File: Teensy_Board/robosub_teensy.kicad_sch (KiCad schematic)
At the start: 51 parts, among them IC1 TEENSY_4.1, J1 Conn_01x03_Pin, J10 Conn_01x02_Pin, J11 Conn_01x02_Pin, J12 Conn_01x04_Pin, J13 Conn_01x04_Pin, J14 Conn_01x04_Pin, J15 Conn_01x04_Pin, J16 Conn_01x04_Pin, J17 Conn_01x04_Pin, J18 Conn_01x04_Pin, J19 Conn_01x04_Pin, J2 Conn_01x03_Pin, J20 Conn_01x04_Pin, J21 Conn_01x04_Pin, J22 Conn_01x06_Pin, J23 Conn_01x06_Pin, J24 Conn_01x06_Pin, J25 Conn_01x01_Pin, J26 Conn_01x01_Pin, J27 Conn_01x01_Pin, J28 Conn_01x01_Pin, J29 Conn_01x01_Pin, J3 Conn_01x03_Pin, J30 Conn_01x01_Pin, J31 Conn_01x01_Pin, J32 Conn_01x01_Pin, J33 Conn_01x01_Pin, J34 Conn_01x01_Pin, J35 Conn_01x01_Pin, J36 Conn_01x01_Pin, J37 Conn_01x01_Pin, J38 Conn_01x01_Pin, J39 Conn_01x01_Pin, J4 Conn_01x03_Pin, J40 Conn_01x01_Pin, J41 Conn_01x01_Pin, J42 Conn_01x01_Pin, J43 Conn_01x01_Pin, J44 Conn_01x01_Pin, J45 Conn_01x01_Pin, J46 Conn_01x01_Pin, J47 Conn_01x01_Pin, J48 Conn_01x10_Pin, J49 Conn_01x10_Pin, J5 Conn_01x03_Pin, J50 Conn_01x10_Pin, J6 Conn_01x03_Pin, J7 Conn_01x03_Pin, J8 Conn_01x03_Pin, J9 Conn_01x02_Pin

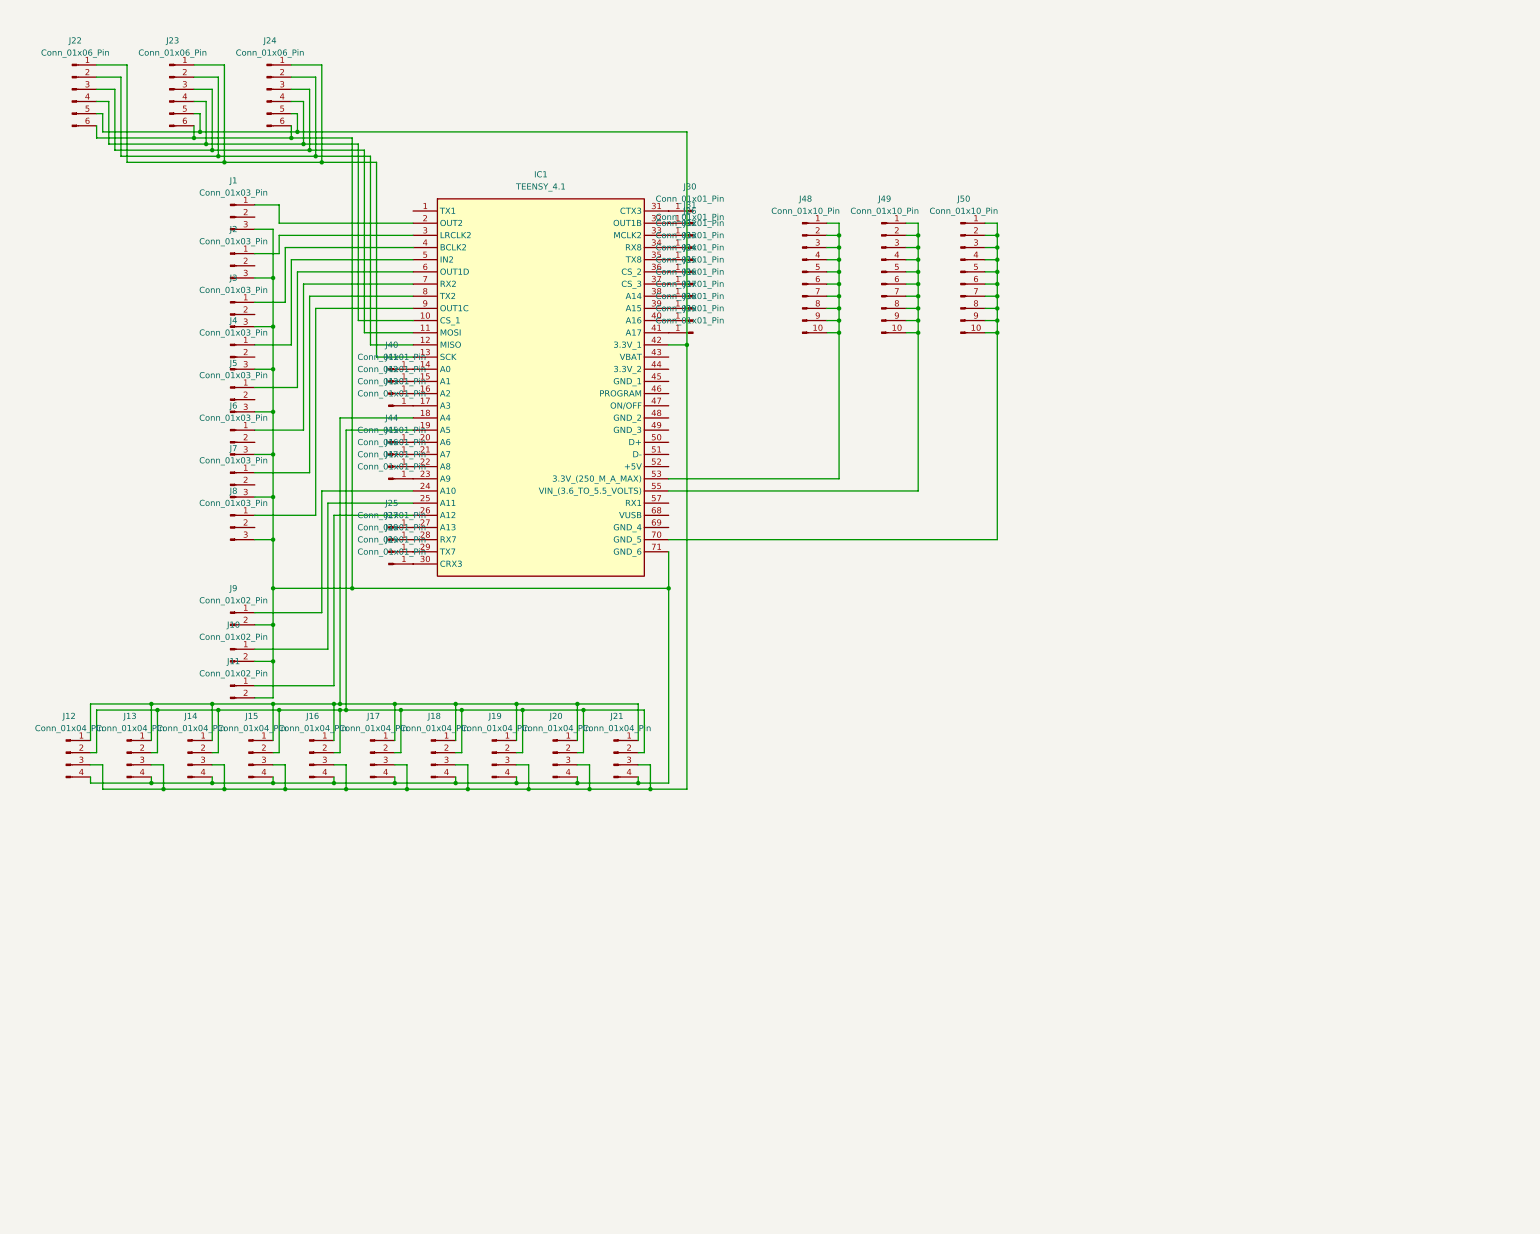
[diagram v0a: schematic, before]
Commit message: teensy board schematic
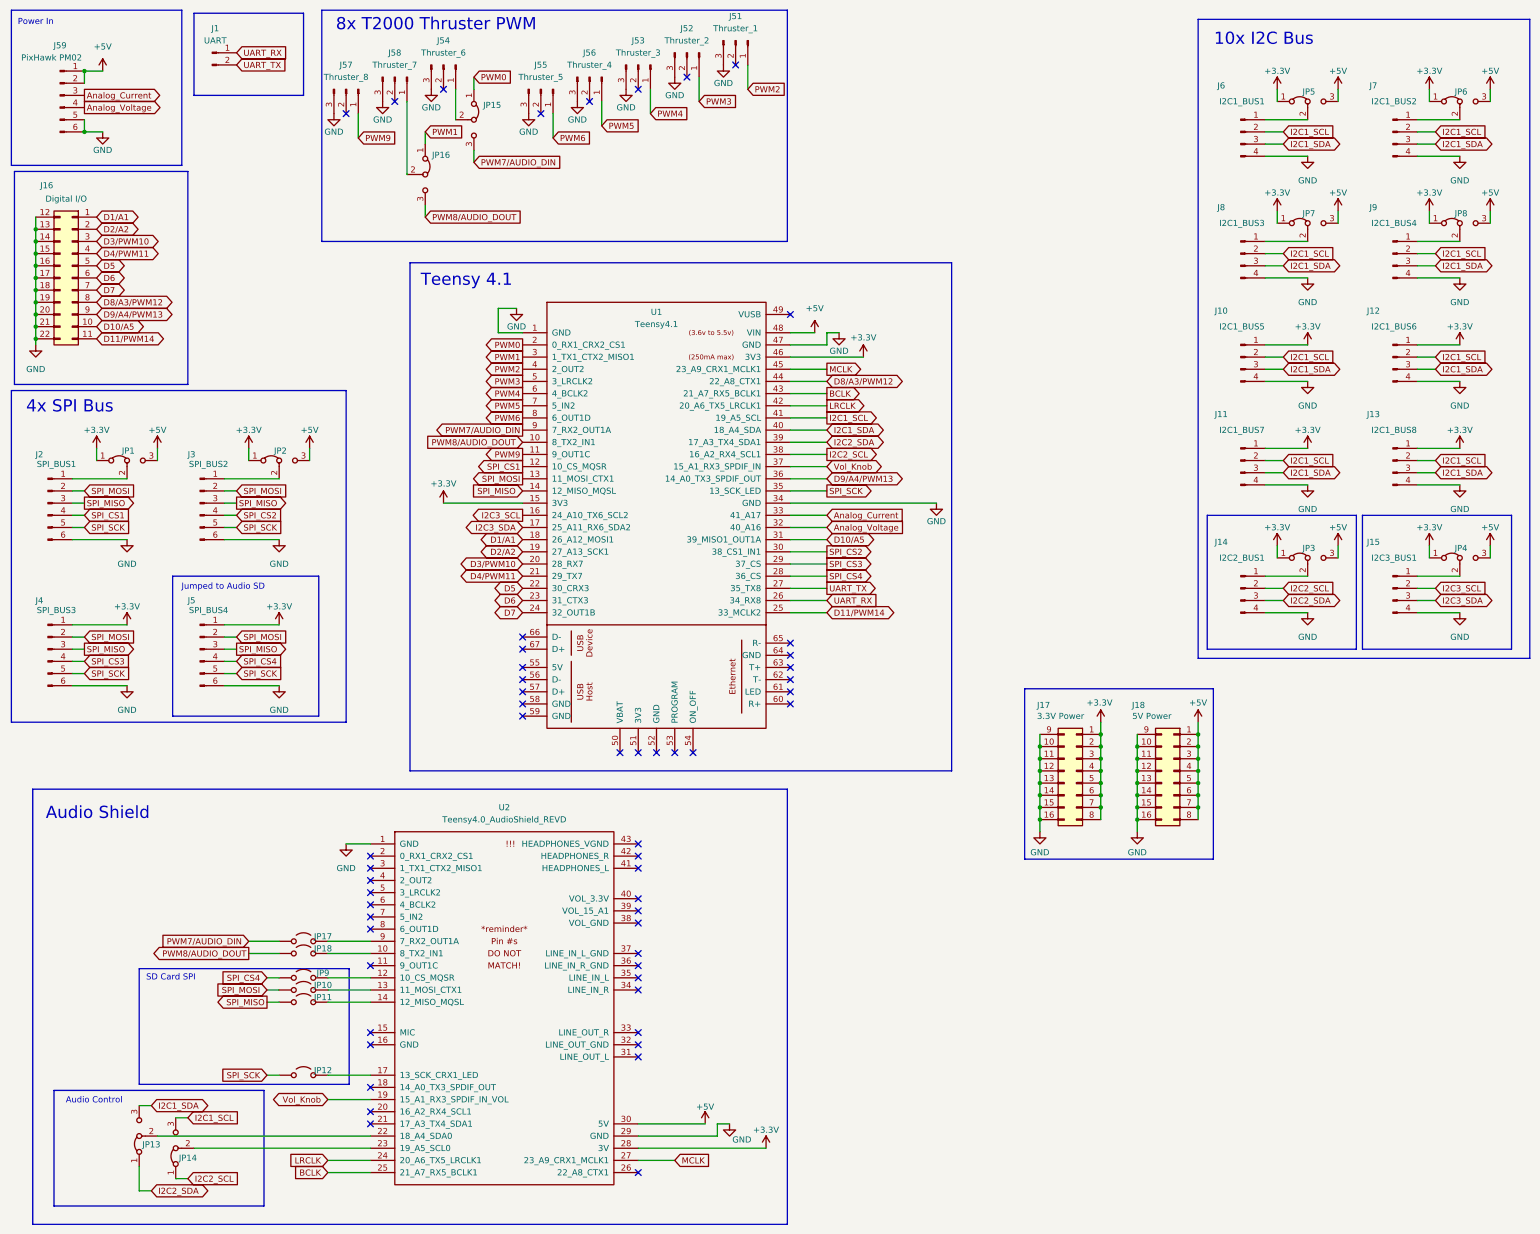
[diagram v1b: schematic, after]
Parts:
- removed IC1: TEENSY_4.1, KiCad:TEENSY41, symbol TEENSY_4_1:TEENSY_4.1
- removed J1, J2, J3, J4, J5, J6, J7, J8: Conn_01x03_Pin, Connector_PinSocket_2.54mm:PinSocket_1x03_P2.54mm_Vertical, symbol Connector:Conn_01x03_Pin
- removed J10, J11, J9: Conn_01x02_Pin, Connector_PinSocket_2.54mm:PinSocket_1x02_P2.54mm_Vertical, symbol Connector:Conn_01x02_Pin
- removed J16, J17, J18, J19, J20, J21: Conn_01x04_Pin, Connector_PinSocket_2.54mm:PinSocket_1x04_P2.54mm_Vertical, symbol Connector:Conn_01x04_Pin
- removed J22, J23, J24: Conn_01x06_Pin, Connector_PinSocket_2.54mm:PinSocket_1x06_P2.54mm_Vertical, symbol Connector:Conn_01x06_Pin
- removed J25, J26, J27, J28, J29, J30, J31, J32, J33, J34, J35, J36, J37, J38, J39, J40, J41, J42, J43, J44, J45, J46, J47: Conn_01x01_Pin, Connector_PinSocket_2.54mm:PinSocket_1x01_P2.54mm_Vertical, symbol Connector:Conn_01x01_Pin
- removed J48, J49, J50: Conn_01x10_Pin, Connector_PinSocket_2.54mm:PinSocket_1x10_P2.54mm_Vertical, symbol Connector:Conn_01x10_Pin
- added J1: UART, Connector_PinSocket_2.54mm:PinSocket_1x02_P2.54mm_Vertical, symbol Connector:Conn_01x02_Pin
- added J10: I2C1_BUS5, Connector_PinSocket_2.54mm:PinSocket_1x04_P2.54mm_Vertical, symbol Connector:Conn_01x04_Pin
- added J11: I2C1_BUS7, Connector_PinSocket_2.54mm:PinSocket_1x04_P2.54mm_Vertical, symbol Connector:Conn_01x04_Pin
- added J16: Digital I/O, symbol Connector_Generic:Conn_02x11_Top_Bottom
- added J17: 3.3V Power, Connector_PinSocket_2.54mm:PinSocket_2x08_P2.54mm_Vertical, symbol Connector_Generic:Conn_02x08_Top_Bottom
- added J18: 5V Power, Connector_PinSocket_2.54mm:PinSocket_2x08_P2.54mm_Vertical, symbol Connector_Generic:Conn_02x08_Top_Bottom
- added J2: SPI_BUS1, Connector_PinSocket_2.54mm:PinSocket_1x06_P2.54mm_Vertical, symbol Connector:Conn_01x06_Pin
- added J3: SPI_BUS2, Connector_PinSocket_2.54mm:PinSocket_1x06_P2.54mm_Vertical, symbol Connector:Conn_01x06_Pin
- added J4: SPI_BUS3, Connector_PinSocket_2.54mm:PinSocket_1x06_P2.54mm_Vertical, symbol Connector:Conn_01x06_Pin
- added J5: SPI_BUS4, Connector_PinSocket_2.54mm:PinSocket_1x06_P2.54mm_Vertical, symbol Connector:Conn_01x06_Pin
- added J51: Thruster_1, Connector_PinSocket_2.54mm:PinSocket_1x03_P2.54mm_Vertical, symbol Connector:Conn_01x03_Pin
- added J52: Thruster_2, Connector_PinSocket_2.54mm:PinSocket_1x03_P2.54mm_Vertical, symbol Connector:Conn_01x03_Pin
- added J53: Thruster_3, Connector_PinSocket_2.54mm:PinSocket_1x03_P2.54mm_Vertical, symbol Connector:Conn_01x03_Pin
- added J54: Thruster_6, Connector_PinSocket_2.54mm:PinSocket_1x03_P2.54mm_Vertical, symbol Connector:Conn_01x03_Pin
- added J55: Thruster_5, Connector_PinSocket_2.54mm:PinSocket_1x03_P2.54mm_Vertical, symbol Connector:Conn_01x03_Pin
- added J56: Thruster_4, Connector_PinSocket_2.54mm:PinSocket_1x03_P2.54mm_Vertical, symbol Connector:Conn_01x03_Pin
- added J57: Thruster_8, Connector_PinSocket_2.54mm:PinSocket_1x03_P2.54mm_Vertical, symbol Connector:Conn_01x03_Pin
- added J58: Thruster_7, Connector_PinSocket_2.54mm:PinSocket_1x03_P2.54mm_Vertical, symbol Connector:Conn_01x03_Pin
- added J59: PixHawk PM02, Connector_PinSocket_2.54mm:PinSocket_1x06_P2.54mm_Vertical, symbol Connector:Conn_01x06_Pin
- added J6: I2C1_BUS1, Connector_PinSocket_2.54mm:PinSocket_1x04_P2.54mm_Vertical, symbol Connector:Conn_01x04_Pin
- added J7: I2C1_BUS2, Connector_PinSocket_2.54mm:PinSocket_1x04_P2.54mm_Vertical, symbol Connector:Conn_01x04_Pin
- added J8: I2C1_BUS3, Connector_PinSocket_2.54mm:PinSocket_1x04_P2.54mm_Vertical, symbol Connector:Conn_01x04_Pin
- added J9: I2C1_BUS4, Connector_PinSocket_2.54mm:PinSocket_1x04_P2.54mm_Vertical, symbol Connector:Conn_01x04_Pin
- added JP1, JP13, JP14, JP15, JP16, JP2, JP3, JP4, JP5, JP6, JP7, JP8: Jumper_3_Bridged12, Connector_PinSocket_2.54mm:PinSocket_1x03_P2.54mm_Vertical, symbol Jumper:Jumper_3_Bridged12
- added JP10, JP11, JP12, JP17, JP18, JP9: Jumper_2_Open, Connector_PinSocket_2.54mm:PinSocket_1x02_P2.54mm_Vertical, symbol Jumper:Jumper_2_Open
- added U1: Teensy4.1, teensy:Teensy41, symbol teensy:Teensy4.1
- added U2: Teensy4.0_AudioShield_REVD, teensy_audio_shield:4.0audioshield, symbol teensy4.0_audioshield_revd:Teensy4.0_AudioShield_REVD
- J12: value Conn_01x04_Pin -> I2C1_BUS6
- J13: value Conn_01x04_Pin -> I2C1_BUS8
- J14: value Conn_01x04_Pin -> I2C2_BUS1
- J15: value Conn_01x04_Pin -> I2C3_BUS1
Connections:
- net +3.3V: now reaches J12.1 (Pin_1), J13.1 (Pin_1)
- net +3.3V: now also J10.1 (Pin_1), J11.1 (Pin_1), J17.1 (Pin_1), J17.2 (Pin_2), J17.3 (Pin_3), J17.4 (Pin_4), J17.5 (Pin_5), J17.6 (Pin_6), J17.7 (Pin_7), J17.8 (Pin_8), J4.1 (Pin_1), J5.1 (Pin_1), JP1.1 (A), JP2.1 (A), JP3.1 (A), JP4.1 (A), JP5.1 (A), JP6.1 (A), JP7.1 (A), JP8.1 (A), U1.15 (3V3), U1.46 (3V3), U2.28 (3V); no longer J14.1 (Pin_1), J15.1 (Pin_1)
- net I2C1_SCL: now reaches J12.2 (Pin_2), J13.2 (Pin_2)
- net I2C1_SCL: now also J10.2 (Pin_2), J11.2 (Pin_2), J6.2 (Pin_2), J7.2 (Pin_2), J8.2 (Pin_2), J9.2 (Pin_2), JP14.3 (B), U1.41 (19_A5_SCL); no longer J14.2 (Pin_2), J15.2 (Pin_2)
- net I2C1_SDA: now reaches J12.3 (Pin_3), J13.3 (Pin_3)
- net I2C1_SDA: now also J10.3 (Pin_3), J11.3 (Pin_3), J6.3 (Pin_3), J7.3 (Pin_3), J8.3 (Pin_3), J9.3 (Pin_3), JP13.3 (B), U1.40 (18_A4_SDA); no longer J14.3 (Pin_3), J15.3 (Pin_3)
- net GND: now reaches J12.4 (Pin_4), J13.4 (Pin_4), J14.4 (Pin_4), J15.4 (Pin_4)
- net GND: now also J10.4 (Pin_4), J11.4 (Pin_4), J16.12 (Pin_12), J16.13 (Pin_13), J16.14 (Pin_14), J16.15 (Pin_15), J16.16 (Pin_16), J16.17 (Pin_17), J16.18 (Pin_18), J16.19 (Pin_19), J16.20 (Pin_20), J16.21 (Pin_21), J16.22 (Pin_22), J17.10 (Pin_10), J17.11 (Pin_11), J17.12 (Pin_12), J17.13 (Pin_13), J17.14 (Pin_14), J17.15 (Pin_15), J17.16 (Pin_16), J17.9 (Pin_9), J18.10 (Pin_10), J18.11 (Pin_11), J18.12 (Pin_12), J18.13 (Pin_13), J18.14 (Pin_14), J18.15 (Pin_15), J18.16 (Pin_16), J18.9 (Pin_9), J2.6 (Pin_6), J3.6 (Pin_6), J4.6 (Pin_6), J5.6 (Pin_6), J51.3 (Pin_3), J52.3 (Pin_3), J53.3 (Pin_3), J54.3 (Pin_3), J55.3 (Pin_3), J56.3 (Pin_3), J57.3 (Pin_3), J58.3 (Pin_3), J59.5 (Pin_5), J59.6 (Pin_6), J6.4 (Pin_4), J7.4 (Pin_4), J8.4 (Pin_4), J9.4 (Pin_4), U1.1 (GND), U1.34 (GND), U1.47 (GND), U2.1 (GND), U2.29 (GND)
- new net: J9.1 (Pin_1), JP8.2 (C)
- new net: J7.1 (Pin_1), JP6.2 (C)
- new net: JP10.2 (B), U2.13 (11_MOSI_CTX1)
- new net: J3.1 (Pin_1), JP2.2 (C)
- new net: JP12.2 (B), U2.17 (13_SCK_CRX1_LED)
- new net: J8.1 (Pin_1), JP7.2 (C)
- new net: JP13.2 (C), U2.22 (18_A4_SDA0)
- new net: J54.1 (Pin_1), JP15.2 (C)
- new net: J15.1 (Pin_1), JP4.2 (C)
- new net: J6.1 (Pin_1), JP5.2 (C)
- new net: J2.1 (Pin_1), JP1.2 (C)
- new net: J14.1 (Pin_1), JP3.2 (C)
- new net: JP14.2 (C), U2.23 (19_A5_SCL0)
- new net: JP11.2 (B), U2.14 (12_MISO_MQSL)
- new net: J58.1 (Pin_1), JP16.2 (C)
- new net: JP9.2 (B), U2.12 (10_CS_MQSR)
- new net: JP17.2 (B), U2.9 (7_RX2_OUT1A)
- new net: JP18.2 (B), U2.10 (8_TX2_IN1)
- new net +5V: J18.1 (Pin_1), J18.2 (Pin_2), J18.3 (Pin_3), J18.4 (Pin_4), J18.5 (Pin_5), J18.6 (Pin_6), J18.7 (Pin_7), J18.8 (Pin_8), J59.1 (Pin_1), J59.2 (Pin_2), JP1.3 (B), JP2.3 (B), JP3.3 (B), JP4.3 (B), JP5.3 (B), JP6.3 (B), JP7.3 (B), JP8.3 (B), U1.48 (VIN), U2.30 (5V)
- new net Analog_Current: J59.3 (Pin_3), U1.33 (41_A17)
- new net Analog_Voltage: J59.4 (Pin_4), U1.32 (40_A16)
- new net BCLK: U1.43 (21_A7_RX5_BCLK1), U2.25 (21_A7_RX5_BCLK1)
- new net D10/A5: J16.10 (Pin_10), U1.31 (39_MISO1_OUT1A)
- new net D11/PWM14: J16.11 (Pin_11), U1.25 (33_MCLK2)
- new net D1/A1: J16.1 (Pin_1), U1.18 (26_A12_MOSI1)
- new net D2/A2: J16.2 (Pin_2), U1.19 (27_A13_SCK1)
- new net D3/PWM10: J16.3 (Pin_3), U1.20 (28_RX7)
- new net D4/PWM11: J16.4 (Pin_4), U1.21 (29_TX7)
- new net D5: J16.5 (Pin_5), U1.22 (30_CRX3)
- new net D6: J16.6 (Pin_6), U1.23 (31_CTX3)
- new net D7: J16.7 (Pin_7), U1.24 (32_OUT1B)
- new net D8/A3/PWM12: J16.8 (Pin_8), U1.44 (22_A8_CTX1)
- new net D9/A4/PWM13: J16.9 (Pin_9), U1.36 (14_A0_TX3_SPDIF_OUT)
- new net I2C2_SCL: J14.2 (Pin_2), JP14.1 (A), U1.38 (16_A2_RX4_SCL1)
- new net I2C2_SDA: J14.3 (Pin_3), JP13.1 (A), U1.39 (17_A3_TX4_SDA1)
- new net I2C3_SCL: J15.2 (Pin_2), U1.16 (24_A10_TX6_SCL2)
- new net I2C3_SDA: J15.3 (Pin_3), U1.17 (25_A11_RX6_SDA2)
- new net LRCLK: U1.42 (20_A6_TX5_LRCLK1), U2.24 (20_A6_TX5_LRCLK1)
- new net MCLK: U1.45 (23_A9_CRX1_MCLK1), U2.27 (23_A9_CRX1_MCLK1)
- new net PWM0: JP15.1 (A), U1.2 (0_RX1_CRX2_CS1)
- new net PWM1: JP16.1 (A), U1.3 (1_TX1_CTX2_MISO1)
- new net PWM2: J51.1 (Pin_1), U1.4 (2_OUT2)
- new net PWM3: J52.1 (Pin_1), U1.5 (3_LRCLK2)
- new net PWM4: J53.1 (Pin_1), U1.6 (4_BCLK2)
- new net PWM5: J56.1 (Pin_1), U1.7 (5_IN2)
- new net PWM6: J55.1 (Pin_1), U1.8 (6_OUT1D)
- new net PWM7/AUDIO_DIN: JP15.3 (B), JP17.1 (A), U1.9 (7_RX2_OUT1A)
- new net PWM8/AUDIO_DOUT: JP16.3 (B), JP18.1 (A), U1.10 (8_TX2_IN1)
- new net PWM9: J57.1 (Pin_1), U1.11 (9_OUT1C)
- new net SPI_CS1: J2.4 (Pin_4), U1.12 (10_CS_MQSR)
- new net SPI_CS2: J3.4 (Pin_4), U1.30 (38_CS1_IN1)
- new net SPI_CS3: J4.4 (Pin_4), U1.29 (37_CS)
- new net SPI_CS4: J5.4 (Pin_4), JP9.1 (A), U1.28 (36_CS)
- new net SPI_MISO: J2.3 (Pin_3), J3.3 (Pin_3), J4.3 (Pin_3), J5.3 (Pin_3), JP11.1 (A), U1.14 (12_MISO_MQSL)
- new net SPI_MOSI: J2.2 (Pin_2), J3.2 (Pin_2), J4.2 (Pin_2), J5.2 (Pin_2), JP10.1 (A), U1.13 (11_MOSI_CTX1)
- new net SPI_SCK: J2.5 (Pin_5), J3.5 (Pin_5), J4.5 (Pin_5), J5.5 (Pin_5), JP12.1 (A), U1.35 (13_SCK_LED)
- new net UART_RX: J1.1 (Pin_1), U1.26 (34_RX8)
- new net UART_TX: J1.2 (Pin_2), U1.27 (35_TX8)
- new net Vol_Knob: U1.37 (15_A1_RX3_SPDIF_IN), U2.19 (15_A1_RX3_SPDIF_IN_VOL)
- no-connect marks 0 -> 54
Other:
- note added: "10x I2C Bus"
- note added: "4x SPI Bus"
- note added: "8x T2000 Thruster PWM"
- note added: "Audio Control"
- note added: "Audio Shield"
- note added: "Jumped to Audio SD"
- note added: "Power In"
- note added: "SD Card SPI"
- note added: "Teensy 4.1"
- company: (none) -> Stanford Robosub
- title: (none) -> Teensy Adapter Board

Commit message: v1 ok2fab
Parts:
- removed J16: Digital I/O, symbol Connector_Generic:Conn_02x11_Top_Bottom
- removed J17: 3.3V Power, Connector_PinSocket_2.54mm:PinSocket_2x08_P2.54mm_Vertical, symbol Connector_Generic:Conn_02x08_Top_Bottom
- removed J18: 5V Power, Connector_PinSocket_2.54mm:PinSocket_2x08_P2.54mm_Vertical, symbol Connector_Generic:Conn_02x08_Top_Bottom
- removed J8: I2C1_BUS3, Connector_PinSocket_2.54mm:PinSocket_1x04_P2.54mm_Vertical, symbol Connector:Conn_01x04_Pin
- removed J9: I2C1_BUS4, Connector_PinSocket_2.54mm:PinSocket_1x04_P2.54mm_Vertical, symbol Connector:Conn_01x04_Pin
- removed JP10, JP11, JP12, JP17, JP18, JP9: Jumper_2_Open, Connector_PinSocket_2.54mm:PinSocket_1x02_P2.54mm_Vertical, symbol Jumper:Jumper_2_Open
- removed JP7, JP8: Jumper_3_Bridged12, Connector_PinSocket_2.54mm:PinSocket_1x03_P2.54mm_Vertical, symbol Jumper:Jumper_3_Bridged12
- added H1, H2, H3: MountingHole, MountingHole:MountingHole_3.2mm_M3, symbol Mechanical:MountingHole
- added J11: 3.3V Power, Connector_PinSocket_2.54mm:PinSocket_2x08_P2.54mm_Vertical, symbol Connector_Generic:Conn_02x08_Odd_Even
- added J12: 5V Power, Connector_PinSocket_2.54mm:PinSocket_2x08_P2.54mm_Vertical, symbol Connector_Generic:Conn_02x08_Odd_Even
- added J17: Digital Pins, Connector_PinSocket_2.54mm:PinSocket_2x11_P2.54mm_Vertical, symbol Connector_Generic:Conn_02x11_Odd_Even
- added JP11: AUDIO_DIN, Jumper:SolderJumper-2_P1.3mm_Open_Pad1.0x1.5mm, symbol Jumper:SolderJumper_2_Open
- added JP12: AUDIO_DOUT, Jumper:SolderJumper-2_P1.3mm_Open_Pad1.0x1.5mm, symbol Jumper:SolderJumper_2_Open
- added JP13: AUDIO_CS, Jumper:SolderJumper-2_P1.3mm_Open_Pad1.0x1.5mm, symbol Jumper:SolderJumper_2_Open
- added JP14: AUDIO_MOSI, Jumper:SolderJumper-2_P1.3mm_Open_Pad1.0x1.5mm, symbol Jumper:SolderJumper_2_Open
- added JP15: AUDIO_MISO, Jumper:SolderJumper-2_P1.3mm_Open_Pad1.0x1.5mm, symbol Jumper:SolderJumper_2_Open
- added JP16: AUDIO_SCK, Jumper:SolderJumper-2_P1.3mm_Open_Pad1.0x1.5mm, symbol Jumper:SolderJumper_2_Open
- J1: renamed from J51; value Thruster_1 -> T1
- J13: renamed from J6; value I2C1_BUS1 -> BUS1
- J14: renamed from J7; value I2C1_BUS2 -> BUS2
- J18: renamed from J10; value I2C1_BUS5 -> BUS3
- J19: renamed from J12; value I2C1_BUS6 -> BUS4
- J20: renamed from J11; value I2C1_BUS7 -> BUS5
- J21: renamed from J13; value I2C1_BUS8 -> BUS6
- J22: renamed from J2; value SPI_BUS1 -> SPI1
- J23: renamed from J3; value SPI_BUS2 -> SPI2
- J24: renamed from J14; value I2C2_BUS1 -> I2C_2
- J25: renamed from J15; value I2C3_BUS1 -> I2C_3
- J26: renamed from J4; value SPI_BUS3 -> SPI3
- J27: renamed from J5; value SPI_BUS4 -> SPI4
- J3: renamed from J52; value Thruster_2 -> T2
- J4: renamed from J54; value Thruster_6 -> T6
- J5: renamed from J53; value Thruster_3 -> T3
- J6: renamed from J58; value Thruster_7 -> T7
- J7: renamed from J56; value Thruster_4 -> T4
- J8: renamed from J57; value Thruster_8 -> T8
- J9: renamed from J55; value Thruster_5 -> T5
- JP1: renamed from JP5; value Jumper_3_Bridged12 -> BUS1_PWR
- JP10: renamed from JP4; value Jumper_3_Bridged12 -> I2C3_PWR
- JP17: renamed from JP13; value Jumper_3_Bridged12 -> SDA_Sel
- JP18: renamed from JP14; value Jumper_3_Bridged12 -> SCL_Sel
- JP2: renamed from JP6; value Jumper_3_Bridged12 -> BUS2_PWR
- JP3: renamed from JP15; value Jumper_3_Bridged12 -> T6_Sel
- JP4: renamed from JP16; value Jumper_3_Bridged12 -> T7_Sel
- JP7: renamed from JP1; value Jumper_3_Bridged12 -> SPI1_PWR
- JP8: renamed from JP2; value Jumper_3_Bridged12 -> SPI2_PWR
- JP9: renamed from JP3; value Jumper_3_Bridged12 -> I2C2_PWR
- renumbered J59 to J10, J1 to J2
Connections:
- net +3.3V: now also J11.10 (Pin_10), J11.12 (Pin_12), J11.14 (Pin_14), J11.16 (Pin_16), J11.2 (Pin_2), J11.4 (Pin_4), J11.6 (Pin_6), J11.8 (Pin_8)
- net +5V: now also J12.10 (Pin_10), J12.12 (Pin_12), J12.14 (Pin_14), J12.16 (Pin_16), J12.2 (Pin_2), J12.4 (Pin_4), J12.6 (Pin_6), J12.8 (Pin_8)
- net D10/A5: now also J17.20 (Pin_20)
- net D11/PWM14: now also J17.22 (Pin_22)
- net D1/A1: now also J17.2 (Pin_2)
- net D2/A2: now also J17.4 (Pin_4)
- net D3/PWM10: now also J17.6 (Pin_6)
- net D4/PWM11: now also J17.8 (Pin_8)
- net D5: now also J17.10 (Pin_10)
- net D6: now also J17.12 (Pin_12)
- net D7: now also J17.14 (Pin_14)
- net D8/A3/PWM12: now also J17.16 (Pin_16)
- net D9/A4/PWM13: now also J17.18 (Pin_18)
- net GND: now also J11.1 (Pin_1), J11.11 (Pin_11), J11.13 (Pin_13), J11.15 (Pin_15), J11.3 (Pin_3), J11.5 (Pin_5), J11.7 (Pin_7), J11.9 (Pin_9), J12.1 (Pin_1), J12.11 (Pin_11), J12.13 (Pin_13), J12.15 (Pin_15), J12.3 (Pin_3), J12.5 (Pin_5), J12.7 (Pin_7), J12.9 (Pin_9), J17.1 (Pin_1), J17.11 (Pin_11), J17.13 (Pin_13), J17.15 (Pin_15), J17.17 (Pin_17), J17.19 (Pin_19), J17.21 (Pin_21), J17.3 (Pin_3), J17.5 (Pin_5), J17.7 (Pin_7), J17.9 (Pin_9)
- net PWM7/AUDIO_DIN: now also JP11.1 (A)
- net PWM8/AUDIO_DOUT: now also JP12.1 (A)
- net SPI_CS4: now also JP13.1 (A)
- net SPI_MISO: now also JP15.1 (A)
- net SPI_MOSI: now also JP14.1 (A)
- net SPI_SCK: now also JP16.1 (A)
- net at U2.13 (11_MOSI_CTX1): now also JP14.2 (B)
- net at U2.17 (13_SCK_CRX1_LED): now also JP16.2 (B)
- net at U2.14 (12_MISO_MQSL): now also JP15.2 (B)
- net at U2.12 (10_CS_MQSR): now also JP13.2 (B)
- net at U2.9 (7_RX2_OUT1A): now also JP11.2 (B)
- net at U2.10 (8_TX2_IN1): now also JP12.2 (B)
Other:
- note added: "8x I2C Bus"
- note removed: "10x I2C Bus"
- moved on the sheet: J18, J19, J20, J21, J24, J25, JP10, JP9
